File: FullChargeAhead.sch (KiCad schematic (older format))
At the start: 15 parts

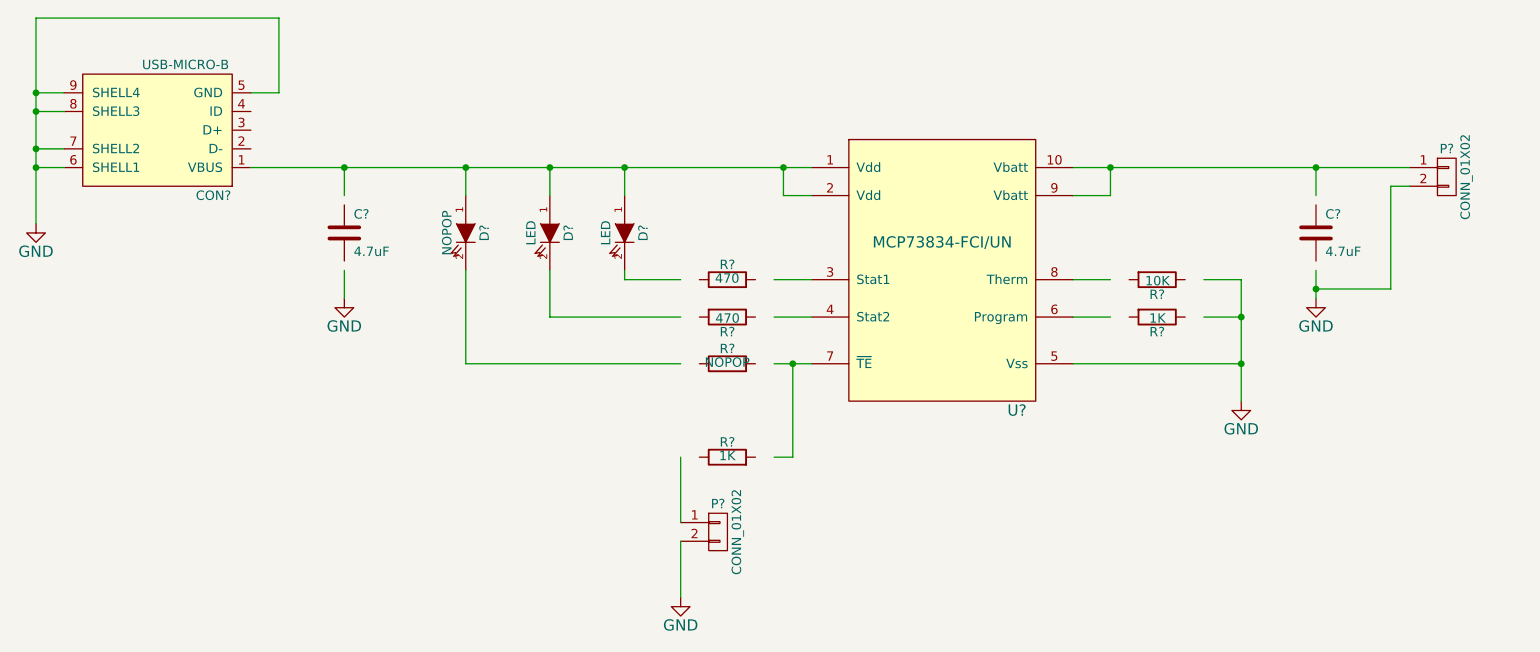
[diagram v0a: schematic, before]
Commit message: Added the new library, created the micro usb foot print and started the layout
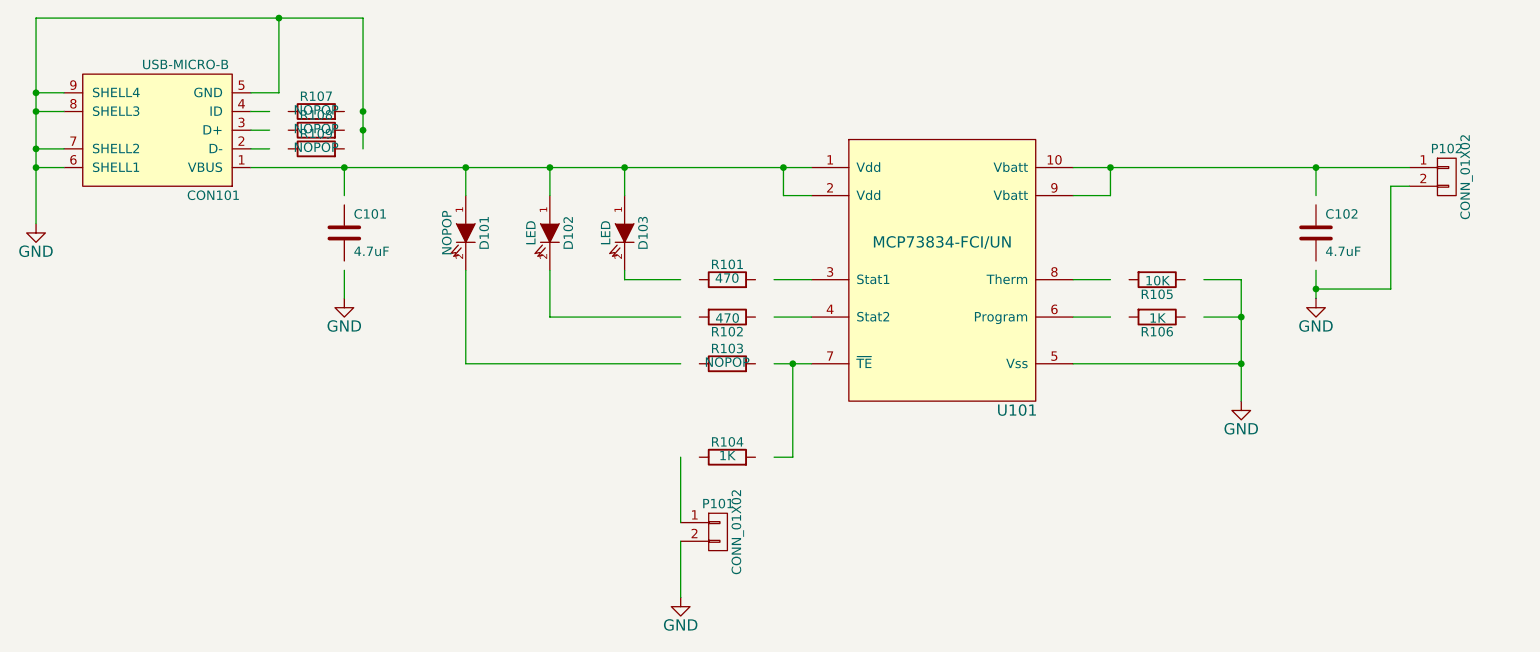
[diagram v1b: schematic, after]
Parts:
- added R107, R108, R109: NOPOP, Resistors_SMD:R_0805_HandSoldering, symbol R
- C101, C102: renamed from C?; footprint (none) -> Capacitors_SMD:C_1206_HandSoldering
- CON101: renamed from CON?; footprint (none) -> fca-lib:USB_Micro_B
- D101, D102, D103: renamed from D?; footprint (none) -> LEDs:LED-0805
- P101, P102: renamed from P?; footprint (none) -> Pin_Headers:Pin_Header_Straight_1x02
- R101, R102, R103, R104, R105, R106: renamed from R?; footprint (none) -> Resistors_SMD:R_0805_HandSoldering
- U101: renamed from U?; footprint (none) -> Housings_SSOP:MSOP-10_3x3mm_Pitch0.5mm
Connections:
- wire segments 58 -> 47
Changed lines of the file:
@@
 $EndDescr
 $Comp
-L MCP73834-FCI/UN U?
+L MCP73834-FCI/UN U101
 U 1 1 550DA710
 P 6900 3350
-F 0 "U?" H 7300 2500 60  0000 C CNN
+F 0 "U101" H 7300 2500 60  0000 C CNN
 F 1 "MCP73834-FCI/UN" H 6900 3400 60  0000 C CNN
-F 2 "" H 6700 3350 60  0000 C CNN
+F 2 "Housings_SSOP:MSOP-10_3x3mm_Pitch0.5mm" H 6700 3350 60  0001 C CNN
 F 3 "" H 6700 3350 60  0000 C CNN
 	1    6900 3350
@@
 $EndComp
 $Comp
-L LED D?
+L LED D101
 U 1 1 550DA792
 P 4350 3250
-F 0 "D?" H 4350 3350 50  0000 C CNN
+F 0 "D101" H 4350 3350 50  0000 C CNN
 F 1 "NOPOP" H 4350 3150 50  0000 C CNN
-F 2 "" H 4350 3250 60  0000 C CNN
+F 2 "LEDs:LED-0805" H 4350 3250 60  0001 C CNN
 F 3 "" H 4350 3250 60  0000 C CNN
 	1    4350 3250
@@
 $EndComp
 $Comp
-L LED D?
+L LED D102
 U 1 1 550DA80B
 P 4800 3250
-F 0 "D?" H 4800 3350 50  0000 C CNN
+F 0 "D102" H 4800 3350 50  0000 C CNN
 F 1 "LED" H 4800 3150 50  0000 C CNN
-F 2 "" H 4800 3250 60  0000 C CNN
+F 2 "LEDs:LED-0805" H 4800 3250 60  0001 C CNN
 F 3 "" H 4800 3250 60  0000 C CNN
 	1    4800 3250
@@
 $EndComp
 $Comp
-L LED D?
+L LED D103
 U 1 1 550DA883
 P 5200 3250
-F 0 "D?" H 5200 3350 50  0000 C CNN
+F 0 "D103" H 5200 3350 50  0000 C CNN
 F 1 "LED" H 5200 3150 50  0000 C CNN
-F 2 "" H 5200 3250 60  0000 C CNN
+F 2 "LEDs:LED-0805" H 5200 3250 60  0001 C CNN
 F 3 "" H 5200 3250 60  0000 C CNN
 	1    5200 3250
@@
 $EndComp
 $Comp
-L R R?
+L R R106
 U 1 1 550DA8D2
 P 8050 3700
-F 0 "R?" V 8130 3700 50  0000 C CNN
+F 0 "R106" V 8130 3700 50  0000 C CNN
 F 1 "1K" V 8057 3701 50  0000 C CNN
-F 2 "" V 7980 3700 30  0000 C CNN
+F 2 "Resistors_SMD:R_0805_HandSoldering" V 7980 3700 30  0001 C CNN
 F 3 "" H 8050 3700 30  0000 C CNN
 	1    8050 3700
@@
 $EndComp
 $Comp
-L R R?
+L R R105
 U 1 1 550DA937
 P 8050 3500
-F 0 "R?" V 8130 3500 50  0000 C CNN
+F 0 "R105" V 8130 3500 50  0000 C CNN
 F 1 "10K" V 8057 3501 50  0000 C CNN
-F 2 "" V 7980 3500 30  0000 C CNN
+F 2 "Resistors_SMD:R_0805_HandSoldering" V 7980 3500 30  0001 C CNN
 F 3 "" H 8050 3500 30  0000 C CNN
 	1    8050 3500
@@
 $EndComp
 $Comp
-L R R?
+L R R103
 U 1 1 550DA9A4
 P 5750 3950
-F 0 "R?" V 5830 3950 50  0000 C CNN
+F 0 "R103" V 5830 3950 50  0000 C CNN
 F 1 "NOPOP" V 5757 3951 50  0000 C CNN
-F 2 "" V 5680 3950 30  0000 C CNN
+F 2 "Resistors_SMD:R_0805_HandSoldering" V 5680 3950 30  0001 C CNN
 F 3 "" H 5750 3950 30  0000 C CNN
 	1    5750 3950
@@
 $EndComp
 $Comp
-L R R?
+L R R102
 U 1 1 550DA9EA
 P 5750 3700
-F 0 "R?" V 5830 3700 50  0000 C CNN
+F 0 "R102" V 5830 3700 50  0000 C CNN
 F 1 "470" V 5757 3701 50  0000 C CNN
-F 2 "" V 5680 3700 30  0000 C CNN
+F 2 "Resistors_SMD:R_0805_HandSoldering" V 5680 3700 30  0001 C CNN
 F 3 "" H 5750 3700 30  0000 C CNN
 	1    5750 3700
@@
 $EndComp
 $Comp
-L R R?
+L R R101
 U 1 1 550DAA1E
 P 5750 3500
-F 0 "R?" V 5830 3500 50  0000 C CNN
+F 0 "R101" V 5830 3500 50  0000 C CNN
 F 1 "470" V 5757 3501 50  0000 C CNN
-F 2 "" V 5680 3500 30  0000 C CNN
+F 2 "Resistors_SMD:R_0805_HandSoldering" V 5680 3500 30  0001 C CNN
 F 3 "" H 5750 3500 30  0000 C CNN
 	1    5750 3500
@@
 $EndComp
 $Comp
-L C C?
+L C C101
 U 1 1 550DAA43
 P 3700 3250
-F 0 "C?" H 3750 3350 50  0000 L CNN
+F 0 "C101" H 3750 3350 50  0000 L CNN
 F 1 "4.7uF" H 3750 3150 50  0000 L CNN
-F 2 "" H 3738 3100 30  0000 C CNN
+F 2 "Capacitors_SMD:C_1206_HandSoldering" H 3738 3100 30  0001 C CNN
 F 3 "" H 3700 3250 60  0000 C CNN
 F 4 "Value" H 3700 3250 60  0001 C CNN "MPN"
@@
 $EndComp
 $Comp
-L C C?
+L C C102
 U 1 1 550DAAE4
 P 8900 3250
-F 0 "C?" H 8950 3350 50  0000 L CNN
+F 0 "C102" H 8950 3350 50  0000 L CNN
 F 1 "4.7uF" H 8950 3150 50  0000 L CNN
-F 2 "" H 8938 3100 30  0000 C CNN
+F 2 "Capacitors_SMD:C_1206_HandSoldering" H 8938 3100 30  0001 C CNN
 F 3 "" H 8900 3250 60  0000 C CNN
 	1    8900 3250
@@
 $EndComp
 Wire Wire Line
-	3200 2900 3700 2900
-Wire Wire Line
-	3700 2900 4350 2900
-Wire Wire Line
-	4350 2900 4800 2900
-Wire Wire Line
-	4800 2900 5200 2900
-Wire Wire Line
-	5200 2900 6050 2900
-Wire Wire Line
-	6050 2900 6200 2900
+	3200 2900 6200 2900
 Wire Wire Line
 	6050 2900 6050 3050
@@
 	6200 3700 6000 3700
 Wire Wire Line
-	6000 3950 6100 3950
-Wire Wire Line
-	6100 3950 6200 3950
-$Comp
-L GND #PWR?
+	6000 3950 6200 3950
+$Comp
+L GND #PWR01
 U 1 1 550DB819
 P 3700 3600
-F 0 "#PWR?" H 3700 3350 60  0001 C CNN
+F 0 "#PWR01" H 3700 3350 60  0001 C CNN
 F 1 "GND" H 3700 3450 60  0000 C CNN
 F 2 "" H 3700 3600 60  0000 C CNN
@@
 	3700 3450 3700 3600
 $Comp
-L GND #PWR?
+L GND #PWR02
 U 1 1 550DBC30
 P 8500 4150
-F 0 "#PWR?" H 8500 3900 60  0001 C CNN
+F 0 "#PWR02" H 8500 3900 60  0001 C CNN
 F 1 "GND" H 8500 4000 60  0000 C CNN
 F 2 "" H 8500 4150 60  0000 C CNN
@@
 $EndComp
 Wire Wire Line
-	7600 2900 7800 2900
-Wire Wire Line
-	7800 2900 8900 2900
-Wire Wire Line
-	8900 2900 9400 2900
+	7600 2900 9400 2900
 Wire Wire Line
 	8900 2900 8900 3050
@@
 	8300 3500 8500 3500
 Wire Wire Line
-	8500 3500 8500 3700
-Wire Wire Line
-	8500 3700 8500 3950
-Wire Wire Line
-	8500 3950 8500 4150
+	8500 3500 8500 4150
 Wire Wire Line
 	8300 3700 8500 3700
 Connection ~ 8500 3700
 Wire Wire Line
-	7600 3700 7800 3700
-Wire Wire Line
 	7600 3950 8500 3950
 Connection ~ 8500 3950
 $Comp
-L GND #PWR?
+L GND #PWR03
 U 1 1 550DC066
 P 8900 3600
-F 0 "#PWR?" H 8900 3350 60  0001 C CNN
+F 0 "#PWR03" H 8900 3350 60  0001 C CNN
 F 1 "GND" H 8900 3450 60  0000 C CNN
 F 2 "" H 8900 3600 60  0000 C CNN
@@
 $EndComp
 Wire Wire Line
-	8900 3450 8900 3550
-Wire Wire Line
-	8900 3550 8900 3600
-$Comp
-L CONN_01X02 P?
+	8900 3450 8900 3600
+$Comp
+L CONN_01X02 P102
 U 1 1 550DC35E
 P 9600 2950
-F 0 "P?" H 9600 3100 50  0000 C CNN
+F 0 "P102" H 9600 3100 50  0000 C CNN
 F 1 "CONN_01X02" V 9700 2950 50  0000 C CNN
-F 2 "" H 9600 2950 60  0000 C CNN
+F 2 "Pin_Headers:Pin_Header_Straight_1x02" H 9600 2950 60  0001 C CNN
 F 3 "" H 9600 2950 60  0000 C CNN
 	1    9600 2950
@@
 Connection ~ 8900 3550
 $Comp
-L R R?
+L R R104
 U 1 1 550DC782
 P 5750 4450
-F 0 "R?" V 5830 4450 50  0000 C CNN
+F 0 "R104" V 5830 4450 50  0000 C CNN
 F 1 "1K" V 5757 4451 50  0000 C CNN
-F 2 "" V 5680 4450 30  0000 C CNN
+F 2 "Resistors_SMD:R_0805_HandSoldering" V 5680 4450 30  0001 C CNN
 F 3 "" H 5750 4450 30  0000 C CNN
 	1    5750 4450
@@
 	5500 4450 5500 4800
 $Comp
-L GND #PWR?
+L GND #PWR04
 U 1 1 550DC8A6
 P 5500 5200
-F 0 "#PWR?" H 5500 4950 60  0001 C CNN
+F 0 "#PWR04" H 5500 4950 60  0001 C CNN
 F 1 "GND" H 5500 5050 60  0000 C CNN
 F 2 "" H 5500 5200 60  0000 C CNN
@@
 $EndComp
 $Comp
-L CONN_01X02 P?
+L CONN_01X02 P101
 U 1 1 550DC9A3
 P 5700 4850
-F 0 "P?" H 5700 5000 50  0000 C CNN
+F 0 "P101" H 5700 5000 50  0000 C CNN
 F 1 "CONN_01X02" V 5800 4850 50  0000 C CNN
-F 2 "" H 5700 4850 60  0000 C CNN
+F 2 "Pin_Headers:Pin_Header_Straight_1x02" H 5700 4850 60  0001 C CNN
 F 3 "" H 5700 4850 60  0000 C CNN
 	1    5700 4850
@@
 	5500 4900 5500 5200
 $Comp
-L USB-MICRO-B CON?
+L USB-MICRO-B CON101
 U 1 1 550DCE37
 P 2700 2700
-F 0 "CON?" H 2400 3050 50  0000 C CNN
+F 0 "CON101" H 2400 3050 50  0000 C CNN
 F 1 "USB-MICRO-B" H 2550 2350 50  0000 C CNN
-F 2 "" H 2700 2600 50  0000 C CNN
+F 2 "fca-lib:USB_Micro_B" H 2700 2600 50  0001 C CNN
 F 3 "" H 2700 2600 50  0000 C CNN
 	1    2700 2700
@@
 $EndComp
 $Comp
-L GND #PWR?
+L GND #PWR05
 U 1 1 550DD3E2
 P 2050 3200
-F 0 "#PWR?" H 2050 2950 60  0001 C CNN
+F 0 "#PWR05" H 2050 2950 60  0001 C CNN
 F 1 "GND" H 2050 3050 60  0000 C CNN
 F 2 "" H 2050 3200 60  0000 C CNN
@@
 	3200 2500 3350 2500
 Wire Wire Line
-	2200 2900 2050 2900
-Wire Wire Line
-	2050 2100 2050 2500
-Wire Wire Line
-	2050 2500 2050 2600
-Wire Wire Line
-	2050 2600 2050 2800
-Wire Wire Line
-	2050 2800 2050 2900
-Wire Wire Line
-	2050 2900 2050 3200
-Wire Wire Line
-	2050 2100 3350 2100
+	2050 2900 2200 2900
+Wire Wire Line
+	2050 2100 2050 3200
+Wire Wire Line
+	2050 2100 3800 2100
 Wire Wire Line
 	2200 2500 2050 2500
@@
 Connection ~ 2050 2800
 Wire Wire Line
-	3350 2100 3350 2500
+	3350 2500 3350 2100
 Connection ~ 2050 2900
+$Comp
+L R R107
+U 1 1 55106E8A
+P 3550 2600
+F 0 "R107" V 3630 2600 50  0000 C CNN
+F 1 "NOPOP" V 3557 2601 50  0000 C CNN
+F 2 "Resistors_SMD:R_0805_HandSoldering" V 3480 2600 30  0001 C CNN
+F 3 "" H 3550 2600 30  0000 C CNN
+	1    3550 2600
+	0    -1   -1   0
+$EndComp
+$Comp
+L R R108
+U 1 1 55106F74
+P 3550 2700
+F 0 "R108" V 3630 2700 50  0000 C CNN
+F 1 "NOPOP" V 3557 2701 50  0000 C CNN
+F 2 "Resistors_SMD:R_0805_HandSoldering" V 3480 2700 30  0001 C CNN
+F 3 "" H 3550 2700 30  0000 C CNN
+	1    3550 2700
+	0    -1   -1   0
+$EndComp
+$Comp
+L R R109
+U 1 1 55106FB8
+P 3550 2800
+F 0 "R109" V 3630 2800 50  0000 C CNN
+F 1 "NOPOP" V 3557 2801 50  0000 C CNN
+F 2 "Resistors_SMD:R_0805_HandSoldering" V 3480 2800 30  0001 C CNN
+F 3 "" H 3550 2800 30  0000 C CNN
+	1    3550 2800
+	0    -1   -1   0
+$EndComp
+Wire Wire Line
+	3200 2600 3300 2600
+Wire Wire Line
+	3200 2700 3300 2700
+Wire Wire Line
+	3200 2800 3300 2800
+Wire Wire Line
+	3800 2100 3800 2800
+Connection ~ 3350 2100
+Connection ~ 3800 2600
+Connection ~ 3800 2700
+Wire Wire Line
+	7600 3700 7800 3700
 $EndSCHEMATC

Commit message: Model update after component resze
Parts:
- renumbered R105 to THERM1
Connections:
- net labels added: Vbat, Vdd
- wire segments 47 -> 51
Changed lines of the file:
@@
 $EndComp
 $Comp
-L R R105
+L R THERM1
 U 1 1 550DA937
 P 8050 3500
-F 0 "R105" V 8130 3500 50  0000 C CNN
+F 0 "THERM1" V 8130 3500 50  0000 C CNN
 F 1 "10K" V 8057 3501 50  0000 C CNN
 F 2 "Resistors_SMD:R_0805_HandSoldering" V 7980 3500 30  0001 C CNN
@@
 Connection ~ 6050 2900
 Wire Wire Line
-	3700 2900 3700 3050
+	3700 2900 3700 3100
 Connection ~ 3700 2900
 Wire Wire Line
@@
 Connection ~ 5200 2900
 Wire Wire Line
-	5500 3500 5200 3500
+	5200 3500 5600 3500
 Wire Wire Line
 	5200 3500 5200 3450
 Wire Wire Line
-	5500 3700 4800 3700
+	4800 3700 5600 3700
 Wire Wire Line
 	4800 3700 4800 3450
 Wire Wire Line
-	5500 3950 4350 3950
+	4350 3950 5600 3950
 Wire Wire Line
 	4350 3950 4350 3450
 Wire Wire Line
-	6200 3500 6000 3500
-Wire Wire Line
-	6200 3700 6000 3700
-Wire Wire Line
-	6000 3950 6200 3950
+	5900 3500 6200 3500
+Wire Wire Line
+	5900 3700 6200 3700
+Wire Wire Line
+	5900 3950 6200 3950
 $Comp
 L GND #PWR01
@@
 $EndComp
 Wire Wire Line
-	3700 3450 3700 3600
+	3700 3400 3700 3600
 $Comp
 L GND #PWR02
@@
 	7600 2900 9400 2900
 Wire Wire Line
-	8900 2900 8900 3050
+	8900 2900 8900 3100
 Connection ~ 8900 2900
 Wire Wire Line
@@
 Connection ~ 7800 2900
 Wire Wire Line
-	7600 3500 7800 3500
-Wire Wire Line
-	8300 3500 8500 3500
+	7600 3500 7900 3500
+Wire Wire Line
+	8200 3500 8500 3500
 Wire Wire Line
 	8500 3500 8500 4150
 Wire Wire Line
-	8300 3700 8500 3700
+	8200 3700 8500 3700
 Connection ~ 8500 3700
 Wire Wire Line
@@
 $EndComp
 Wire Wire Line
-	8900 3450 8900 3600
+	8900 3400 8900 3600
 $Comp
 L CONN_01X02 P102
@@
 $EndComp
 Wire Wire Line
-	6100 3950 6100 4450
-Wire Wire Line
-	6100 4450 6000 4450
+	6100 4450 6100 3950
+Wire Wire Line
+	5900 4450 6100 4450
 Connection ~ 6100 3950
 Wire Wire Line
@@
 $EndComp
 Wire Wire Line
-	3200 2600 3300 2600
-Wire Wire Line
-	3200 2700 3300 2700
-Wire Wire Line
-	3200 2800 3300 2800
+	3200 2600 3400 2600
+Wire Wire Line
+	3200 2700 3400 2700
+Wire Wire Line
+	3200 2800 3400 2800
 Wire Wire Line
 	3800 2100 3800 2800
@@
 Connection ~ 3800 2700
 Wire Wire Line
-	7600 3700 7800 3700
+	7600 3700 7900 3700
+Text Label 4950 2900 0    60   ~ 0
+Vdd
+Text Label 8200 2900 0    60   ~ 0
+Vbat
+Wire Wire Line
+	3800 2800 3700 2800
+Wire Wire Line
+	3700 2700 3800 2700
+Wire Wire Line
+	3700 2600 3800 2600
+Wire Wire Line
+	5500 4450 5600 4450
 $EndSCHEMATC

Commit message: Preperation for layout
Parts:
- P102: footprint Pin_Headers:Pin_Header_Straight_1x02 -> fca-lib:JST_2Pin; ConradPN (none) -> 740197-62; MPN (none) -> S2B-PH-K-S
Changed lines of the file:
@@
 P 9600 2950
 F 0 "P102" H 9600 3100 50  0000 C CNN
-F 1 "CONN_01X02" V 9700 2950 50  0000 C CNN
-F 2 "Pin_Headers:Pin_Header_Straight_1x02" H 9600 2950 60  0001 C CNN
+F 1 "CONN_01X02" H 9750 2800 50  0000 C CNN
+F 2 "fca-lib:JST_2Pin" H 9600 2950 60  0001 C CNN
 F 3 "" H 9600 2950 60  0000 C CNN
+F 4 "S2B-PH-K-S" H 9600 2950 60  0001 C CNN "MPN"
+F 5 "740197-62" H 9600 2950 60  0001 C CNN "ConradPN"
 	1    9600 2950
 	1    0    0    -1
@@
 P 5700 4850
 F 0 "P101" H 5700 5000 50  0000 C CNN
-F 1 "CONN_01X02" V 5800 4850 50  0000 C CNN
+F 1 "CONN_01X02" H 5800 4650 50  0000 C CNN
 F 2 "Pin_Headers:Pin_Header_Straight_1x02" H 5700 4850 60  0001 C CNN
 F 3 "" H 5700 4850 60  0000 C CNN

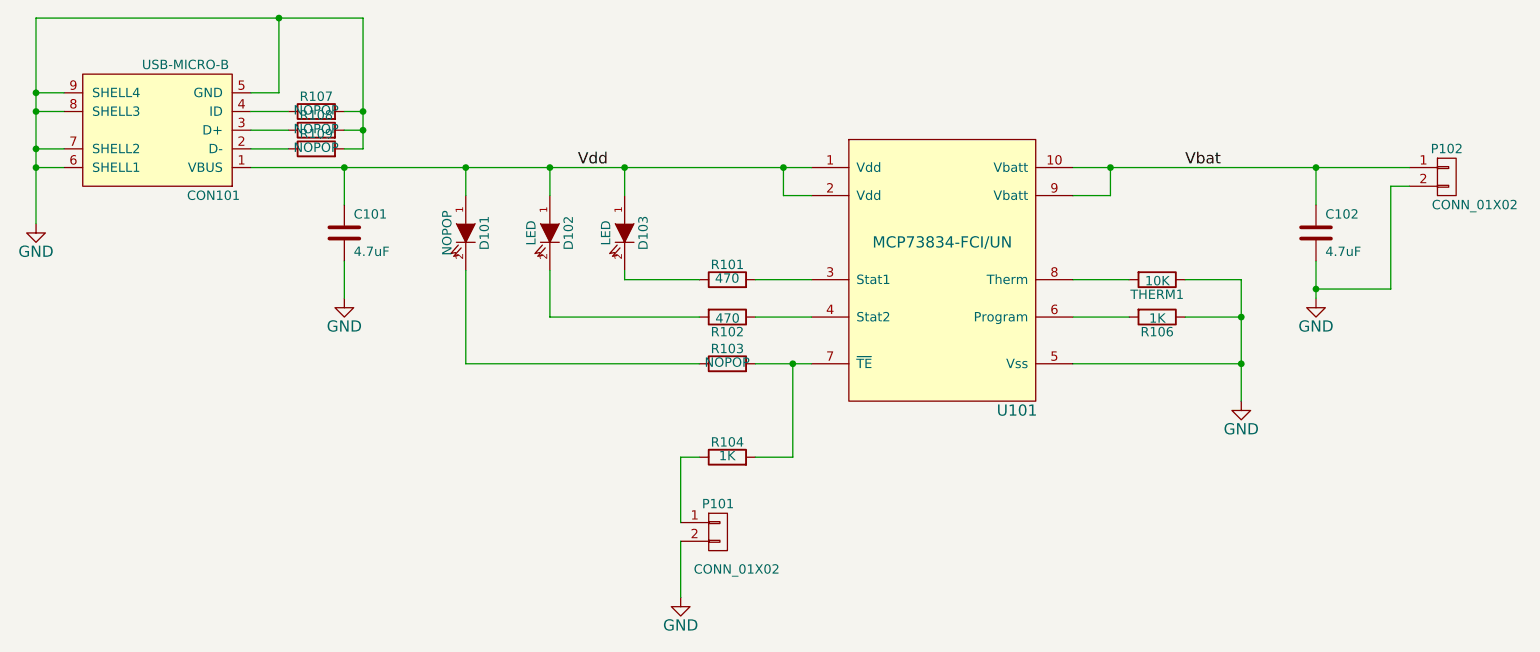
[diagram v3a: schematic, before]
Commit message: Corrected the footprint for the JST connector
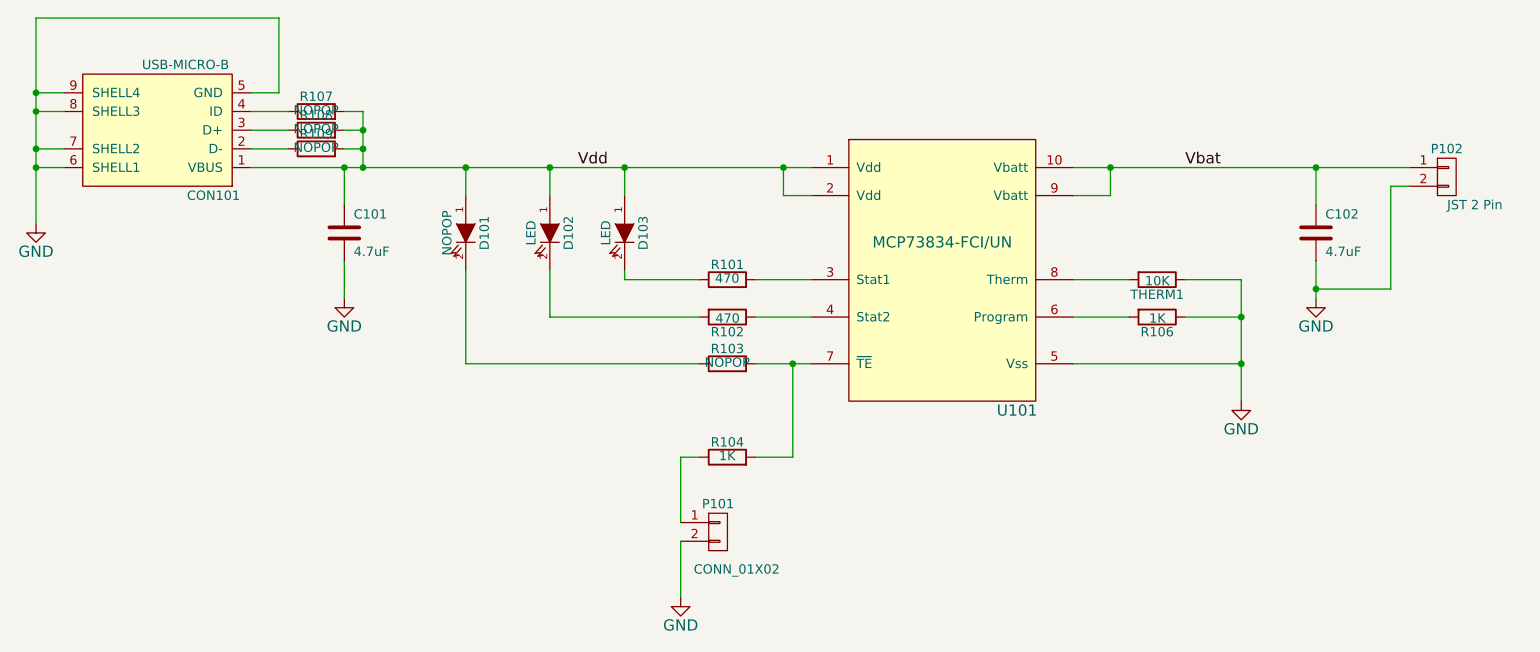
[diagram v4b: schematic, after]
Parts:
- P102: value CONN_01X02 -> JST 2 Pin
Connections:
- net GND: no longer R107.2, R108.2, R109.2
- net Vdd: now also R107.2, R108.2, R109.2
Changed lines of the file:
@@
 P 9600 2950
 F 0 "P102" H 9600 3100 50  0000 C CNN
-F 1 "CONN_01X02" H 9750 2800 50  0000 C CNN
+F 1 "JST 2 Pin" H 9750 2800 50  0000 C CNN
 F 2 "fca-lib:JST_2Pin" H 9600 2950 60  0001 C CNN
 F 3 "" H 9600 2950 60  0000 C CNN
@@
 	2050 2100 2050 3200
 Wire Wire Line
-	2050 2100 3800 2100
-Wire Wire Line
 	2200 2500 2050 2500
 Connection ~ 2050 2500
@@
 Wire Wire Line
 	3200 2800 3400 2800
-Wire Wire Line
-	3800 2100 3800 2800
-Connection ~ 3350 2100
-Connection ~ 3800 2600
 Connection ~ 3800 2700
 Wire Wire Line
@@
 	3700 2700 3800 2700
 Wire Wire Line
+	5500 4450 5600 4450
+Connection ~ 3800 2900
+Connection ~ 3800 2800
+Wire Wire Line
+	3350 2100 2050 2100
+Wire Wire Line
+	3800 2600 3800 2900
+Wire Wire Line
 	3700 2600 3800 2600
-Wire Wire Line
-	5500 4450 5600 4450
 $EndSCHEMATC
